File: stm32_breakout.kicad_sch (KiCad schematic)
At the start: 7 parts, among them J4 USB_C_Receptacle_USB2.0_16P, U7 STM32H743ZGTx, Y1 SG-310 32MHz

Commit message: add tcxo 32MHz clock
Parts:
- removed Y1: SG-310 32MHz, Crystal:Crystal_SMD_3225-4Pin_3.2x2.5mm, symbol Oscillator:SG-210STF
- added C51, C54, C55: 100nF, symbol Device:C_Small
- added C52: 1nF, symbol Device:C_Small
- added R15: 1M, symbol Device:R_Small_US
- added R16: 22, symbol Device:R_Small_US
- added U3: 74LVC1GU04, Package_TO_SOT_SMD:SOT-353_SC-70-5, symbol 74xGxx:74LVC1GU04
- added U9: 74LVC1G04, Package_TO_SOT_SMD:SOT-353_SC-70-5, symbol 74xGxx:74LVC1G04
- added Y1: 32MHz TCXO, Crystal:Crystal_SMD_2016-4Pin_2.0x1.6mm, symbol Oscillator:TG2520SMN-xx.xxxxxxMhz-xxxxNM
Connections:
- net GND: now also C51.1, C54.2, C55.2, U3.3 (GND), U9.3 (GND), Y1.2 (GND)
- new net: C52.2, R15.1, U3.2
- new net: R15.2, U3.4, U9.2
- new net: C52.1, Y1.3 (OUT)
- new net: R16.1, U9.4
- new net +3.3V: C51.2, C54.1, C55.1, U3.5 (VCC), U9.5 (VCC), Y1.4 (Vcc)
- new net 32 MHz: R16.2
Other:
- note added: "32 MHz CMOS from clipped sine"
- note added: "Bias resistor"
- note added: "Buffered inverter to square waveform"
- note added: "Unbuffered inverter, ~20x gain"
- moved on the sheet: C22, CR1, J4, R25, R26, U7

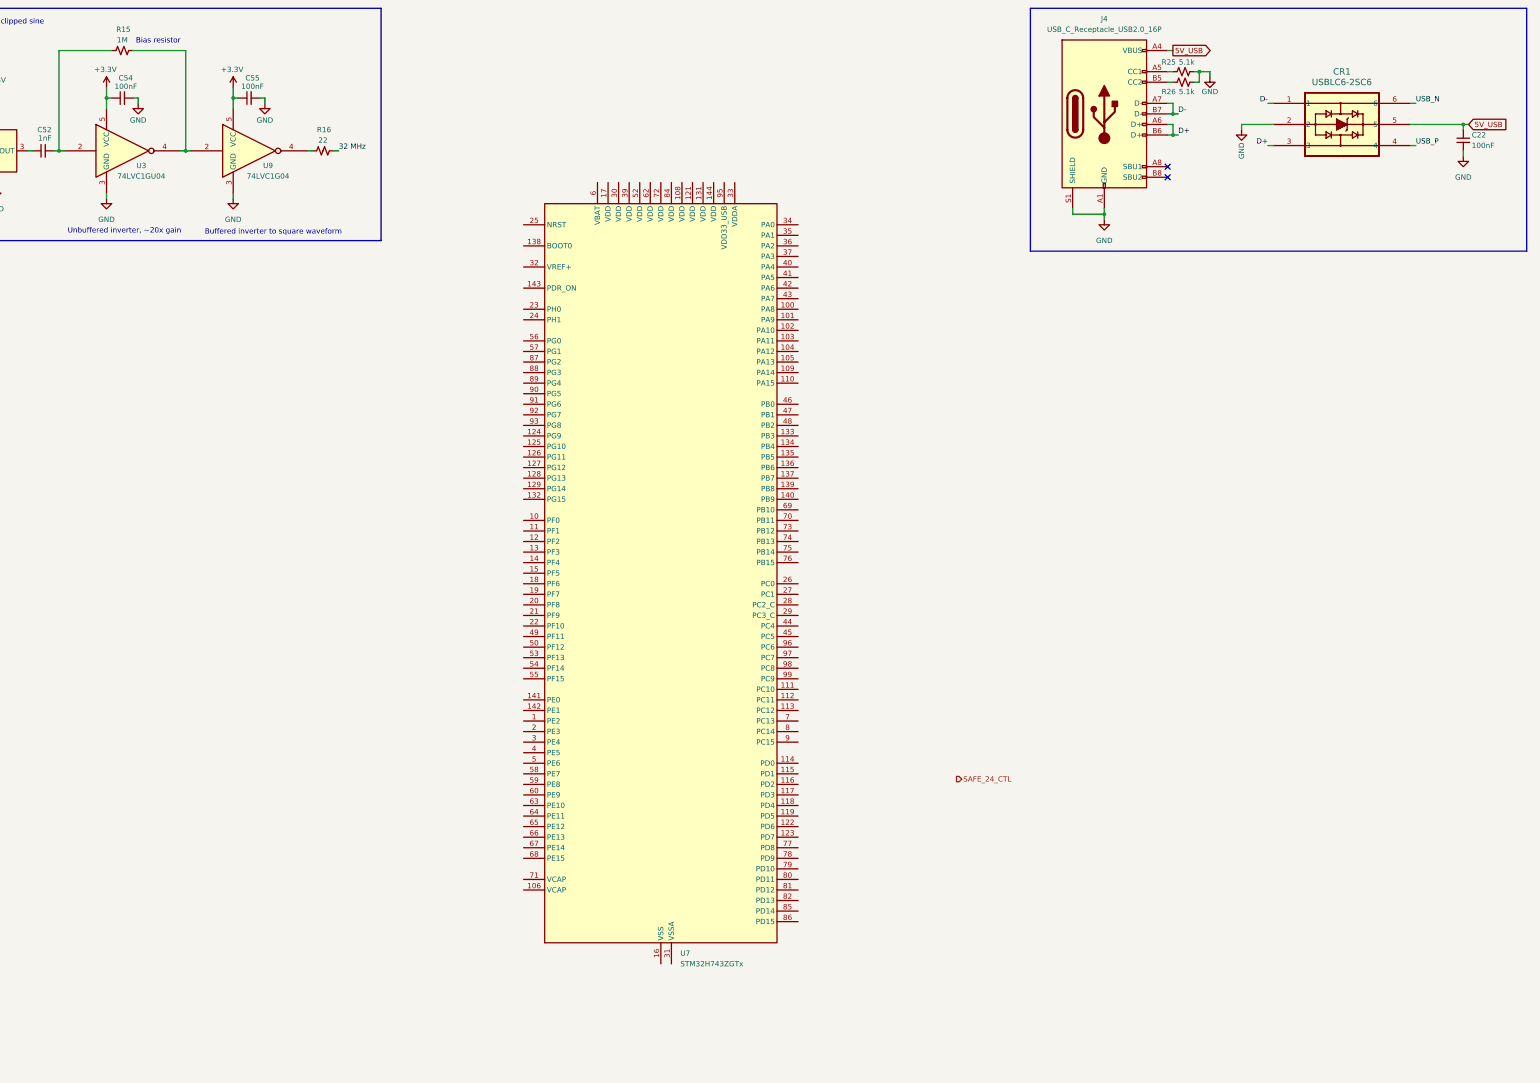
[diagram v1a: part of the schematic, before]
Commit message: add ethernet phy to rj45
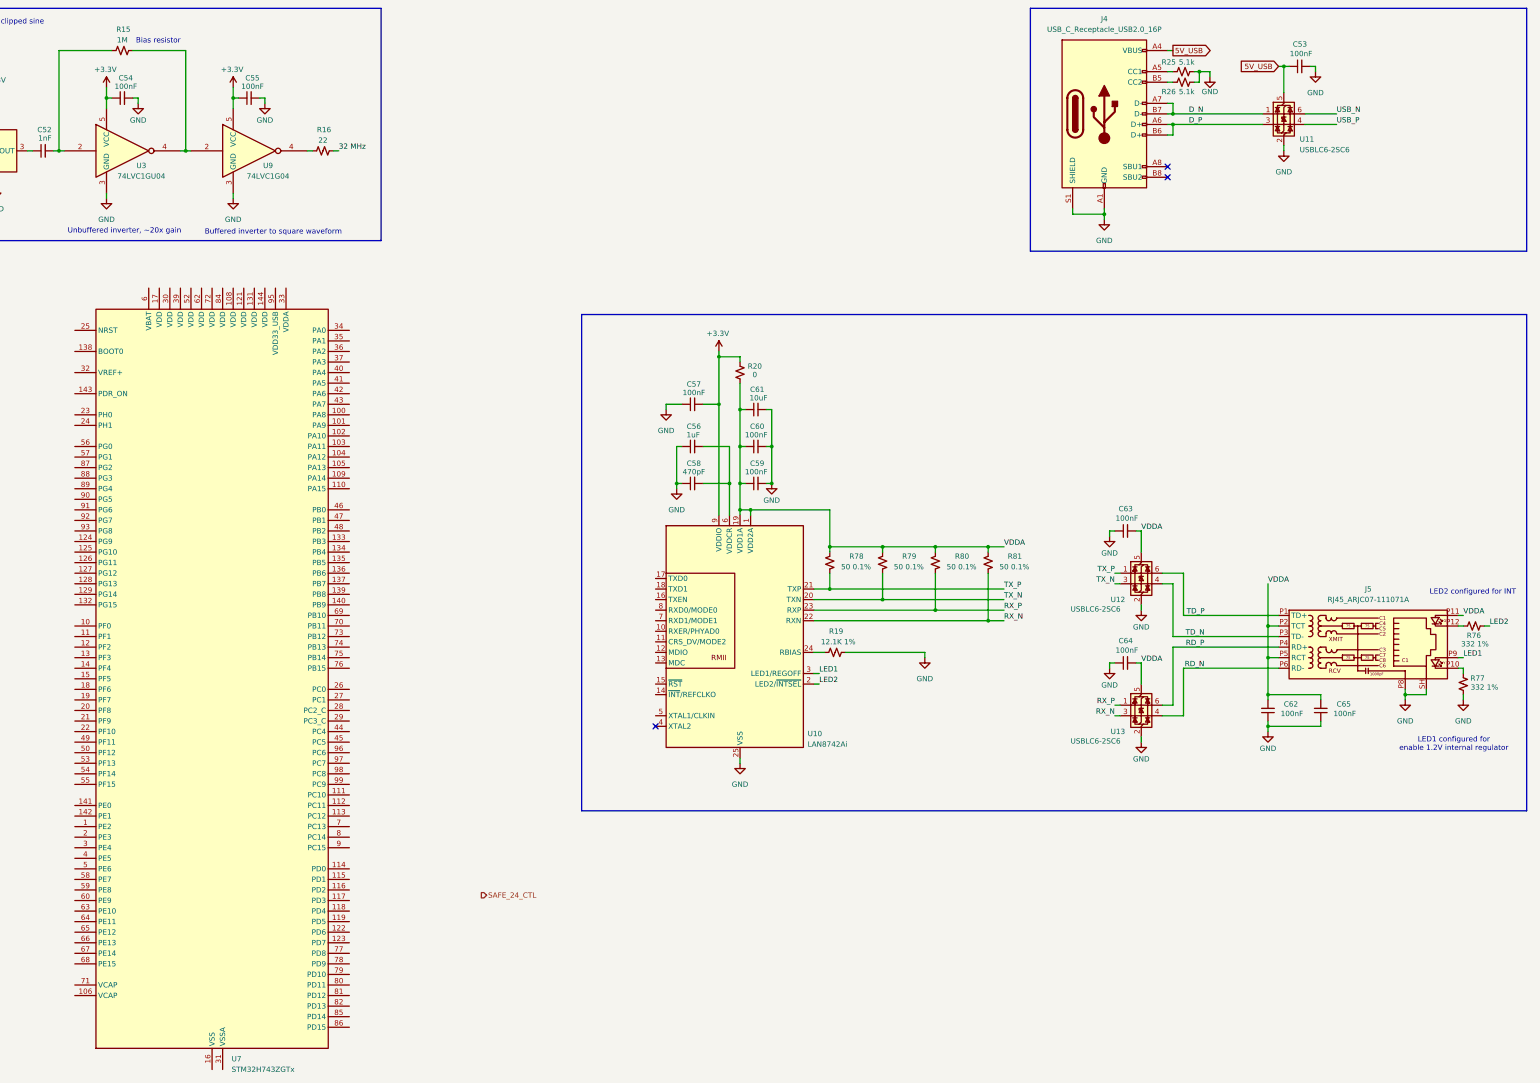
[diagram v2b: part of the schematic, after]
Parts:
- removed C22: 100nF, symbol Device:C_Small
- removed CR1: USBLC6-2SC6, Package_TO_SOT_SMD:SOT-23-6, symbol USBLC6-2SC6:USBLC6-2SC6
- added C53, C57, C59, C60, C62, C63, C64, C65: 100nF, symbol Device:C_Small
- added C56: 1uF, symbol Device:C_Small
- added C58: 470pF, symbol Device:C_Small
- added C61: 10uF, symbol Device:C_Small
- added J5: RJ45_ARJC07-111071A, symbol Connector:RJ45_Bel_SI-60062-F
- added R19: 12.1K 1%, symbol Device:R_Small_US
- added R20: 0, symbol Device:R_Small_US
- added R76, R77: 332 1%, symbol Device:R_Small_US
- added R78, R79, R80, R81: 50 0.1%, Resistor_SMD:R_0603_1608Metric, symbol Device:R_Small_US
- added U10: LAN8742Ai, Package_DFN_QFN:VQFN-24-1EP_4x4mm_P0.5mm_EP2.5x2.5mm_ThermalVias, symbol Interface_Ethernet:LAN8742A
- added U11, U12, U13: USBLC6-2SC6, Package_TO_SOT_SMD:SOT-23-6, symbol Power_Protection:USBLC6-2SC6
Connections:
- net +3.3V: now also C57.2, R20.1, U10.9 (VDDIO)
- net 5V_USB: now also C53.1, U11.5 (VBUS)
- net GND: now also C53.2, C56.1, C57.1, C58.1, C59.2, C60.2, C61.2, C62.1, C63.1, C64.1, C65.1, J5.P8, J5.SH, R19.2, R77.2, U10.25 (VSS), U11.2 (GND), U12.2 (GND), U13.2 (GND)
- net USB_N: now also U11.6 (I/O1)
- net USB_P: now also U11.4 (I/O2)
- net D+ renamed D_P
- net D_P: now also U11.3 (I/O2)
- net D- renamed D_N
- net D_N: now also U11.1 (I/O1)
- new net: C56.2, C58.2, U10.6 (VDDCR)
- new net: J5.P12, R76.2
- new net: R19.1, U10.24 (RBIAS)
- new net: J5.P10, R77.1
- new net LED1: J5.P9, U10.3 (LED1/REGOFF)
- new net LED2: R76.1, U10.2 (LED2/~{INTSEL})
- new net RD_N: J5.P6 (RD-), U13.4 (I/O2)
- new net RD_P: J5.P4 (RD+), U13.6 (I/O1)
- new net RX_N: R81.1, U10.22 (RXN), U13.3 (I/O2)
- new net RX_P: R80.1, U10.23 (RXP), U13.1 (I/O1)
- new net TD_N: J5.P3 (TD-), U12.4 (I/O2)
- new net TD_P: J5.P1 (TD+), U12.6 (I/O1)
- new net TX_N: R79.1, U10.20 (TXN), U12.3 (I/O2)
- new net TX_P: R78.1, U10.21 (TXP), U12.1 (I/O1)
- new net VDDA: C59.1, C60.1, C61.1, C62.2, C63.2, C64.2, C65.2, J5.P11, J5.P2 (TCT), J5.P5 (RCT), R20.2, R78.2, R79.2, R80.2, R81.2, U10.1 (VDD2A), U10.19 (VDD1A), U12.5 (VBUS), U13.5 (VBUS)
- no-connect marks 2 -> 3
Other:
- note added: "LED1 configured for enable 1.2V internal regulator"
- note added: "LED2 configured for INT"
- moved on the sheet: U7
